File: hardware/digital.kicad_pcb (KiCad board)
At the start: 4 copper layers, 186.7 x 100 mm, 515 parts, among them J1 IPEX-1, J10 Conn_01x03_Pin, J11 Conn_01x03_Pin, J12 Conn_01x10_Pin, J14 Conn_01x03_Pin, J15 Conn_01x02_Pin, J16 Conn_01x03_Pin, J17 Micro_SD_Card_Det1, J18 Conn_01x03_Pin, J19 Micro_SD_Card_Det1, J2 IPEX-1, J20 USB_C_Receptacle_USB2.0_16P, J21 USB_C_Receptacle_USB2.0_16P, J22 USB_C_Receptacle_USB2.0_16P, J23 IPEX-1, J24 IPEX-1, J25 IPEX-1, J26 IPEX-1, J27 IPEX-1, J28 IPEX-1, J29 IPEX-1, J3 IPEX-1, J30 IPEX-1, J35 IPEX-1, J36 IPEX-1, J37 IPEX-1, J38 IPEX-1, J39 IPEX-1, J4 IPEX-1, J40 IPEX-1, J41 IPEX-1, J42 IPEX-1, J43 IPEX-1, J44 IPEX-1, J45 IPEX-1, J46 IPEX-1, J47 IPEX-1, J48 IPEX-1, J49 IPEX-1, J5 IPEX-1, J50 IPEX-1, J51 IPEX-1, J52 IPEX-1, J53 IPEX-1, J54 IPEX-1, J55 IPEX-1, J56 IPEX-1, J57 IPEX-1, J58 IPEX-1, J6 IPEX-1, J7 IPEX-1, J8 IPEX-1, J9 IPEX-1, Q1 BSC098N10NS5, Q2 BSC098N10NS5, SW1 SW_DIP_x03, SW2 SW_DIP_x03, SW3 SW_DIP_x03, SW4 SW_DIP_x03, SW5 SW_DIP_x03, SW6 SW_DIP_x03, SW7 SW_DIP_x03, U1 ICE40HX4K-TQ144, U10 LM5050-1, U11 CH224K, U12 LM5050-1, U13 CH224K, U14 TPS54302, U15 TPS7A7002DDA, U16 TPS54302, U17 TPS7A7002DDA, U18 74HC244, U19 74HC244, U2 74HC244, U20 74HC244, U21 REF5030ID, U22 MCP4728, U23 MCP4728, U24 REF5050ID, U25 MCP4728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

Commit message: route
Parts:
- removed the C62 at (66.5, 118.7)
- removed the C63 at (66.5, 122.8)
- removed the C64 at (76.0, 123.7)
- removed the C65 at (78.5, 123.2)
- removed the C66 at (43.5, 117.2)
- removed the C69 at (76.0, 139.2)
- removed the C70 at (78.5, 138.7)
- removed the C72 at (64.8, 105.8)
- removed the C73 at (59.7, 108.3)
- removed the C74 at (61.4, 108.3)
- removed the C75 at (68.3, 104.3)
- removed the C76 at (60.1, 105.2)
- removed the C77 at (60.1, 103.7)
- removed the C78 at (52.9, 99.5)
- removed the C79 at (54.6, 99.6)
- removed the C80 at (67.4, 99.5)
- removed the C81 at (64.2, 102.2)
- removed the C82 at (113.6, 212.3)
- removed the C83 at (113.6, 215.3)
- removed the C84 at (113.6, 218.4)
- removed the C85 at (64.8, 89.9)
- removed the C86 at (59.7, 92.4)
- removed the C87 at (61.4, 92.4)
- removed the C88 at (68.3, 88.4)
- removed the C89 at (60.1, 89.3)
- removed the C90 at (60.1, 87.8)
- removed the C91 at (52.8, 83.8)
- removed the C92 at (54.5, 83.8)
- removed the C93 at (67.3, 83.5)
- removed the C94 at (64.1, 86.3)
- removed the C95 at (113.6, 221.4)
- removed the C96 at (113.6, 224.4)
- removed the C97 at (113.6, 227.4)
- removed the D11 at (37.5, 118.1)
- removed the D12 at (69.5, 119.7)
- removed the D13 at (51.5, 119.2)
- removed the D14 at (48.5, 119.2)
- removed the D16 at (69.5, 134.7)
- removed the D18 at (76.5, 128.7)
- removed the J20 at (32.0, 121.2)
- removed the J23 at (100.5, 196.8)
- removed the J24 at (100.5, 206.1)
- removed the J25 at (109.9, 196.8)
- removed the J26 at (109.9, 206.1)
- removed the J27 at (119.3, 196.8)
- removed the J28 at (119.3, 206.1)
- removed the J29 at (128.7, 196.8)
- removed the J30 at (128.7, 206.1)
- removed JP3, JP4, JP5: SolderJumper_2_Open, Jumper:SolderJumper-2_P1.3mm_Open_RoundedPad1.0x1.5mm
- removed L4, L5: 10uH, Inductor_SMD:L_Changjiang_FXL0630
- removed Q1, Q2: BSC098N10NS5, Package_TO_SOT_SMD:TDSON-8-1
- removed the R52 at (50.0, 117.2)
- removed the R53 at (40.5, 117.7)
- removed the R54 at (51.5, 116.7)
- removed the R57 at (48.5, 116.7)
- removed the R58 at (53.0, 118.7)
- removed the R59 at (53.0, 121.2)
- removed the R60 at (53.0, 123.7)
- removed the R61 at (79.1, 128.7)
- removed the R69 at (67.3, 104.3)
- removed the R70 at (64.7, 99.0)
- removed the R71 at (64.7, 100.5)
- removed the R72 at (64.8, 110.8)
- removed the R73 at (66.3, 104.3)
- removed the R74 at (64.8, 104.8)
- removed the R75 at (64.7, 97.5)
- removed the R76 at (64.8, 103.8)
- removed the R77 at (67.3, 88.4)
- removed the R78 at (64.6, 82.9)
- removed the R79 at (64.6, 84.4)
- removed the R80 at (64.8, 94.9)
- removed the R81 at (66.3, 88.4)
- removed the R82 at (64.8, 88.9)
- removed the R83 at (64.6, 81.4)
- removed the R84 at (64.8, 87.9)
- removed the SW1 at (59.5, 121.2)
- removed the U10 at (73.0, 123.7)
- removed the U11 at (43.5, 121.2)
- removed the U12 at (73.0, 139.2)
- removed the U14 at (64.8, 108.3)
- removed the U15 at (59.2, 99.5)
- removed the U16 at (64.8, 92.4)
- removed the U17 at (59.1, 83.5)
- moved R24 54.4 mm to (91.5, 104.1), turned to -90 degrees
- moved C29 52.3 mm to (91.5, 92.0), turned to 0 degrees
- moved JP1 52.0 mm to (89.7, 104.2), turned to 90 degrees
- moved C28 51.9 mm to (91.5, 95.8), turned to 0 degrees
- moved C34 49.5 mm to (89.0, 88.5), turned to 90 degrees
- moved R28 48.9 mm to (88.8, 101.0), turned to 90 degrees
- moved C33 48.1 mm to (88.0, 88.5), turned to 90 degrees
- moved C40 47.8 mm to (87.4, 104.1), turned to 90 degrees
- moved C32 47.3 mm to (84.2, 79.6), turned to 90 degrees
- moved R26 46.7 mm to (87.0, 88.5), turned to -90 degrees
- moved C24 46.2 mm to (86.9, 101.0), turned to -90 degrees
- moved R25 45.3 mm to (86.0, 88.5), turned to -90 degrees
- moved C31 44.8 mm to (85.9, 101.0), turned to -90 degrees
- moved JP2 44.7 mm to (81.8, 79.3), turned to 180 degrees
- moved Y1 44.3 mm to (84.8, 104.1), turned to 0 degrees
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- renumbered C6 to C10, C130 to C100, C131 to C101, C132 to C102, C133 to C103, C134 to C104, C135 to C105, C136 to C106, C137 to C107, C138 to C108, C139 to C109, C7 to C11, C140 to C110, C141 to C111, C142 to C112, C143 to C113, C144 to C114, C145 to C115, C146 to C116, C149 to C12, C8 to C13, C10 to C14, C11 to C15, C13 to C16, C14 to C17, C15 to C18, C16 to C19, C17 to C20, C18 to C21, C19 to C22, C20 to C23, C21 to C24, C22 to C25, C23 to C26, C24 to C27, C25 to C28, C26 to C29, C148 to C3, C27 to C30, C28 to C31, C29 to C32, C30 to C33, C31 to C34, C32 to C35, C33 to C36, C34 to C37, C35 to C38, C36 to C39, C3 to C4, C37 to C40, C38 to C41, C39 to C42, C40 to C43, C41 to C44, C42 to C45, C43 to C46, C44 to C47, C45 to C48, C46 to C49, C147 to C5, C47 to C50, C48 to C51, C49 to C52, C50 to C53, C51 to C54, C52 to C55, C53 to C56, C54 to C57, C55 to C58, C56 to C59, C4 to C6, C57 to C60, C58 to C61, C59 to C62, C60 to C63, C61 to C64, C67 to C65, C68 to C66, C71 to C67, C98 to C68, C99 to C69, C12 to C7, C100 to C70, C101 to C71, C102 to C72, C103 to C73, C104 to C74, C105 to C75, C106 to C76, C107 to C77, C108 to C78, C109 to C79, C5 to C8, C110 to C80, C111 to C81, C112 to C82, C113 to C83, C114 to C84, C115 to C85, C116 to C86, C117 to C87, C118 to C88, C119 to C89, C120 to C90, C121 to C91, C122 to C92, C123 to C93, C124 to C94, C125 to C95, C126 to C96, C127 to C97, C128 to C98, C129 to C99, D15 to D10, D17 to D11, D19 to D12, D10 to D13, D20 to D14, D21 to D15, D22 to D16, D23 to D17, D24 to D18, D25 to D19, D26 to D20, D27 to D21, D28 to D22, D29 to D23, D30 to D24, D31 to D25, D32 to D26, D33 to D27, D34 to D28, D35 to D29, D36 to D30, D37 to D31, D38 to D32, D39 to D33, D40 to D34, D41 to D35, D42 to D36, D43 to D37, J14 to J13, J15 to J14, J16 to J15, J17 to J16, J18 to J17, J19 to J18, J22 to J19, J21 to J20, J35 to J21, J36 to J22, J37 to J23, J38 to J24, J39 to J25, J40 to J26, J41 to J27, J42 to J28, J43 to J29, J44 to J30, J45 to J31, J46 to J32, J47 to J33, J48 to J34, J49 to J35, J50 to J36, J51 to J37, J52 to J38, J53 to J39, J54 to J40, J55 to J41, J56 to J42, J57 to J43, J58 to J44, R124 to R100, R125 to R101, R126 to R102, R127 to R103, R128 to R104, R129 to R105, R130 to R106, R131 to R107, R132 to R108, R133 to R109, R134 to R110, R135 to R111, R136 to R112, R137 to R113, R138 to R114, R139 to R115, R140 to R116, R141 to R117, R142 to R118, R143 to R119, R144 to R120, R145 to R121, R146 to R122, R147 to R123, R148 to R124, R149 to R125, R150 to R126, R151 to R127, R152 to R128, R153 to R129, R154 to R130, R155 to R131, R156 to R132, R157 to R133, R158 to R134, R159 to R135, R160 to R136, R62 to R51, R63 to R52, R64 to R53, R65 to R54, R66 to R55, R67 to R56, R68 to R57, R51 to R58, R55 to R59, R56 to R60, R85 to R61, R86 to R62, R87 to R63, R88 to R64, R89 to R65, R90 to R66, R91 to R67, R92 to R68, R93 to R69, R94 to R70, R95 to R71, R96 to R72, R97 to R73, R98 to R74, R99 to R75, R100 to R76, R101 to R77, R102 to R78, R103 to R79, R104 to R80, R105 to R81, R106 to R82, R107 to R83, R108 to R84, R109 to R85, R110 to R86, R111 to R87, R112 to R88, R113 to R89, R114 to R90, R115 to R91, R116 to R92, R117 to R93, R118 to R94, R119 to R95, R120 to R96, R121 to R97, R122 to R98, R123 to R99, SW2 to SW1, SW3 to SW2, SW4 to SW3, SW5 to SW4, SW6 to SW5, SW7 to SW6, TP43 to TP1, TP22 to TP10, TP4 to TP11, TP23 to TP12, TP24 to TP13, TP5 to TP14, TP25 to TP15, TP6 to TP16, TP26 to TP17, TP7 to TP18, TP27 to TP19, TP44 to TP2, TP28 to TP20, TP29 to TP21, TP30 to TP22, TP8 to TP23, TP16 to TP24, TP9 to TP25, TP31 to TP26, TP10 to TP27, TP32 to TP28, TP33 to TP29, TP1 to TP3, TP34 to TP30, TP11 to TP31, TP35 to TP32, TP36 to TP33, TP12 to TP34, TP37 to TP35, TP13 to TP36, TP38 to TP37, TP14 to TP38, TP18 to TP4, TP15 to TP43, TP17 to TP44, TP2 to TP5, TP3 to TP6, TP19 to TP7, TP20 to TP8, TP21 to TP9, U13 to U10, U18 to U11, U19 to U12, U20 to U13, U21 to U14, U22 to U15, U23 to U16, U24 to U17, U25 to U18, U26 to U19, U27 to U20, U28 to U21, U29 to U22, U30 to U23, U31 to U24, U32 to U25, U33 to U26, U34 to U27, U35 to U28, U36 to U29, U37 to U30, U38 to U31, U39 to U32, U40 to U33, U41 to U34, U42 to U35, U43 to U36, U44 to U37, U45 to U38
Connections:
- C65 pad 1: Net-(D15-K) -> +20V
- C66 pad 1: Net-(D15-K) -> +20V
- D10 pad 1: Net-(D15-K) -> +20V
- J19 pad A4: Net-(D15-K) -> +20V
- J19 pad A9: Net-(D15-K) -> +20V
- J19 pad B4: Net-(D15-K) -> +20V
- J19 pad B9: Net-(D15-K) -> +20V
- R51 pad 1: Net-(D15-K) -> +20V
- R52 pad 1: Net-(D15-K) -> +20V
- R53 pad 1: Net-(D15-K) -> +20V
- U4 pad 4: /MCU/~{LDAC}0 -> /MCU/~{LDAC}5
- U4 pad 5: /MCU/~{LDAC}1 -> /MCU/~{LDAC}4
- U4 pad 6: /MCU/~{LDAC}2 -> /MCU/~{LDAC}3
- U4 pad 7: /MCU/~{LDAC}3 -> /MCU/~{LDAC}2
- U4 pad 8: /MCU/~{LDAC}4 -> /MCU/~{LDAC}1
- U4 pad 9: /MCU/~{LDAC}5 -> /MCU/~{LDAC}0
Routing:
- net /MCU/~{LDAC}2: track 0.00 -> 118.8 mm, vias 0 -> 2
- net /MCU/~{LDAC}3: track 0.00 -> 111.4 mm, vias 0 -> 2
- net /MCU/~{LDAC}1: track 0.00 -> 108.2 mm, vias 0 -> 2
- net /MCU/~{LDAC}4: track 0.00 -> 106.4 mm, vias 0 -> 2
- net +5V5_A: track 0.00 -> 98.8 mm
- net /MCU/~{LDAC}0: track 0.00 -> 85.9 mm, vias 0 -> 2
- net /MCU/~{LDAC}5: track 0.00 -> 80.4 mm, vias 0 -> 2
- net /MCU/SD_SO: track 0.00 -> 50.9 mm, vias 0 -> 3
- net /FPGA/GBIN2: track 0.00 -> 49.0 mm, vias 0 -> 2
- net /FPGA/D3: track 0.00 -> 39.2 mm, vias 0 -> 2
- net /FPGA/CDONE: track 0.00 -> 37.5 mm, vias 0 -> 2
- net /FPGA/D1: track 0.00 -> 37.4 mm, vias 0 -> 2
- net /MCU/SD_SI: track 0.00 -> 36.6 mm, vias 0 -> 2
- net /FPGA/~{RESET}: track 0.00 -> 36.4 mm, vias 0 -> 2
- net /FPGA/D2: track 0.00 -> 36.0 mm, vias 0 -> 2
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
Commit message: route all signal
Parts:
- removed A1: RaspberryPi_Pico, Module:RaspberryPi_Pico_SMD_HandSolder
- removed R79: 0R, Resistor_SMD:R_0402_1005Metric
- added J45: Conn_01x24_Pin, Connector_PinHeader_2.54mm:PinHeader_1x24_P2.54mm_Vertical, F.Cu at (137.2, 56.0)
- added TP45: TestPoint, TestPoint:TestPoint_Pad_D1.0mm, B.Cu at (117.0, 87.0)
- added TP46: TestPoint, TestPoint:TestPoint_Pad_D1.0mm, B.Cu at (115.0, 87.0)
- moved TP4 42.5 mm to (181.0, 115.0)
- moved TP24 42.4 mm to (181.0, 85.0), turned to -90 degrees
- moved R17 25.4 mm to (108.2, 97.5), turned to 180 degrees
- moved C97 6.52 mm to (151.0, 74.8), turned to 90 degrees
- moved TP44 6.21 mm to (98.4, 109.7)
- moved C80 5.48 mm to (179.0, 125.2), turned to -90 degrees
- moved C79 5.10 mm to (176.0, 123.0), turned to 180 degrees
- moved C89 4.49 mm to (190.2, 86.0), turned to 0 degrees
- moved TP7 2.94 mm to (139.5, 128.9), turned to 146.25 degrees
- moved TP19 2.76 mm to (193.8, 125.2), turned to -123.75 degrees
- moved TP8 2.69 mm to (148.0, 134.5), turned to 146.25 degrees
- moved C77 2.14 mm to (155.0, 125.2), turned to -90 degrees
- moved TP13 2.02 mm to (177.0, 136.2), turned to -168.75 degrees
- moved TP20 2.02 mm to (199.2, 117.0), turned to -123.75 degrees
- moved J1 1.97 mm to (116.5, 117.5)
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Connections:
- net /debug/CH_0 renamed Net-(U11-1Y0)
- net /debug/CH_1 renamed Net-(U11-1Y1)
- net /debug/CH_10 renamed Net-(U12-1Y2)
- net /debug/CH_11 renamed Net-(U12-1Y3)
- net /debug/CH_12 renamed Net-(U12-2Y0)
- net /debug/CH_13 renamed Net-(U12-2Y1)
- net /debug/CH_14 renamed Net-(U12-2Y2)
- net /debug/CH_15 renamed Net-(U12-2Y3)
- net /debug/CH_16 renamed Net-(U13-1Y0)
- net /debug/CH_17 renamed Net-(U13-1Y1)
- net /debug/CH_18 renamed Net-(U13-1Y2)
- net /debug/CH_19 renamed Net-(U13-1Y3)
- net /debug/CH_2 renamed Net-(U11-1Y2)
- net /debug/CH_20 renamed Net-(U13-2Y0)
- net /debug/CH_21 renamed Net-(U13-2Y1)
- net /debug/CH_22 renamed Net-(U13-2Y2)
- net /debug/CH_23 renamed Net-(U13-2Y3)
- net /debug/CH_3 renamed Net-(U11-1Y3)
- net /debug/CH_4 renamed Net-(U11-2Y0)
- net /debug/CH_5 renamed Net-(U11-2Y1)
- net /debug/CH_6 renamed Net-(U11-2Y2)
- net /debug/CH_7 renamed Net-(U11-2Y3)
- net /debug/CH_8 renamed Net-(U12-1Y0)
- net /debug/CH_9 renamed Net-(U12-1Y1)
- C68 pad 2: +3V3_DEBUG -> +3V3
- C69 pad 2: +3V3_DEBUG -> +3V3
- C70 pad 2: +3V3_DEBUG -> +3V3
- C71 pad 2: +3V3_DEBUG -> +3V3
- C72 pad 2: +3V3_DEBUG -> +3V3
- C73 pad 2: +3V3_DEBUG -> +3V3
- U1 pad 33: /FPGA/DEBUG_TRIG_0 -> Net-(U1D-IOL_25A)
- U1 pad 34: /FPGA/DEBUG_TRIG_1 -> Net-(U1D-IOL_25B)
- U11 pad 20: +3V3_DEBUG -> +3V3
- U12 pad 20: +3V3_DEBUG -> +3V3
- U13 pad 20: +3V3_DEBUG -> +3V3
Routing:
- net /MCU/VREF_SDA: track 2.60 -> 213.6 mm, vias 0 -> 7
- net /MCU/VREF_SCL: track 2.35 -> 209.4 mm, vias 0 -> 7
- net /FPGA/DEBUG_0: track 0.00 -> 60.3 mm, vias 0 -> 2
- net /FPGA/DEBUG_1: track 0.00 -> 58.8 mm, vias 0 -> 2
- net /FPGA/DEBUG_2: track 0.00 -> 57.7 mm, vias 0 -> 2
- net /FPGA/DEBUG_23: track 0.00 -> 57.6 mm, vias 0 -> 2
- net /FPGA/DEBUG_3: track 0.00 -> 56.7 mm, vias 0 -> 2
- net /FPGA/DEBUG_22: track 0.00 -> 55.9 mm, vias 0 -> 2
- net /FPGA/DEBUG_21: track 0.00 -> 54.3 mm, vias 0 -> 2
- net /FPGA/DEBUG_20: track 0.00 -> 53.8 mm, vias 0 -> 2
- net /FPGA/DEBUG_19: track 0.00 -> 53.7 mm, vias 0 -> 2
- net /FPGA/DEBUG_18: track 0.00 -> 53.2 mm, vias 0 -> 2
- net /FPGA/DEBUG_4: track 0.00 -> 52.6 mm, vias 0 -> 2
- net /FPGA/DEBUG_17: track 0.00 -> 52.3 mm, vias 0 -> 2
- net /FPGA/DEBUG_16: track 0.00 -> 51.6 mm, vias 0 -> 2
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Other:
- board size 186.7 x 100 mm -> 162.2 x 100 mm

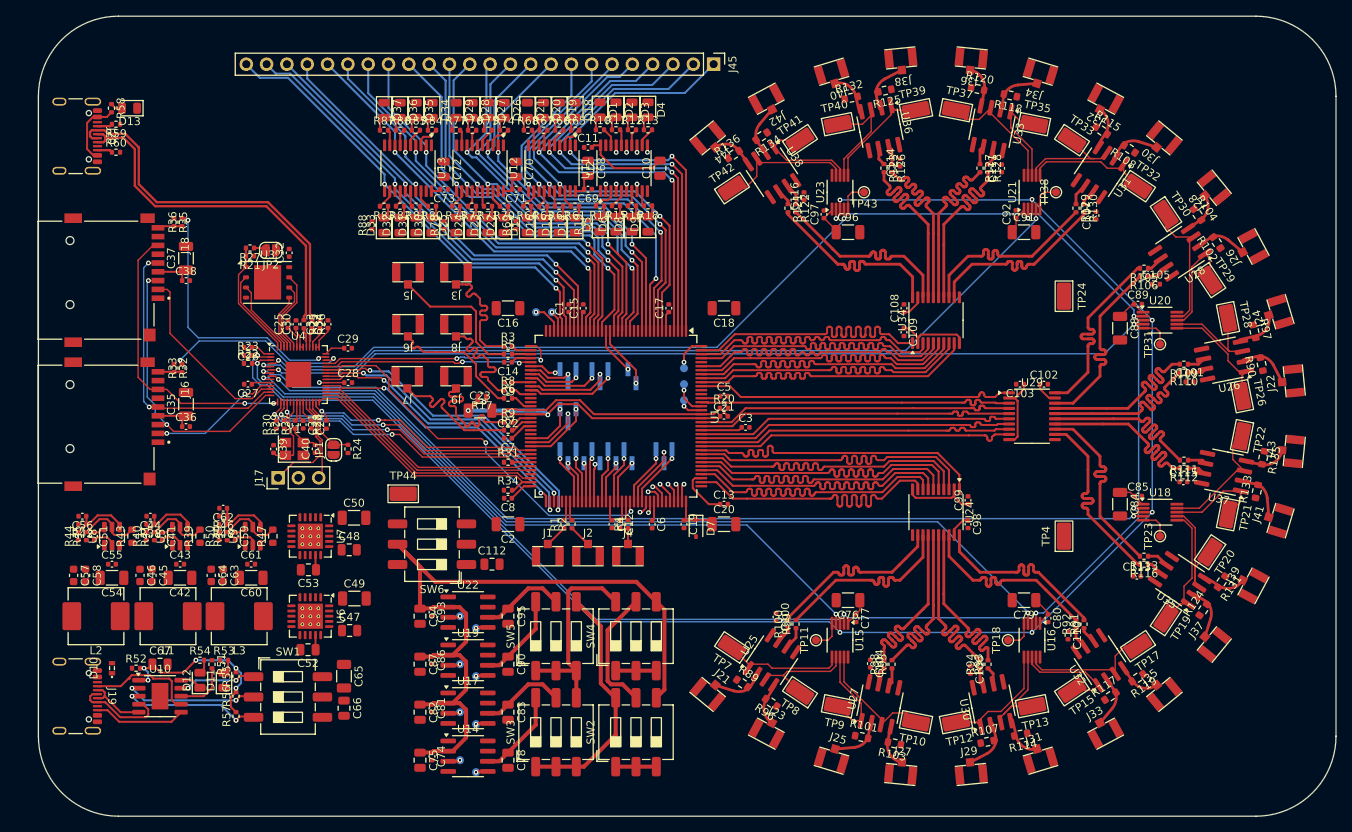
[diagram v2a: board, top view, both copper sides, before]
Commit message: add board edge
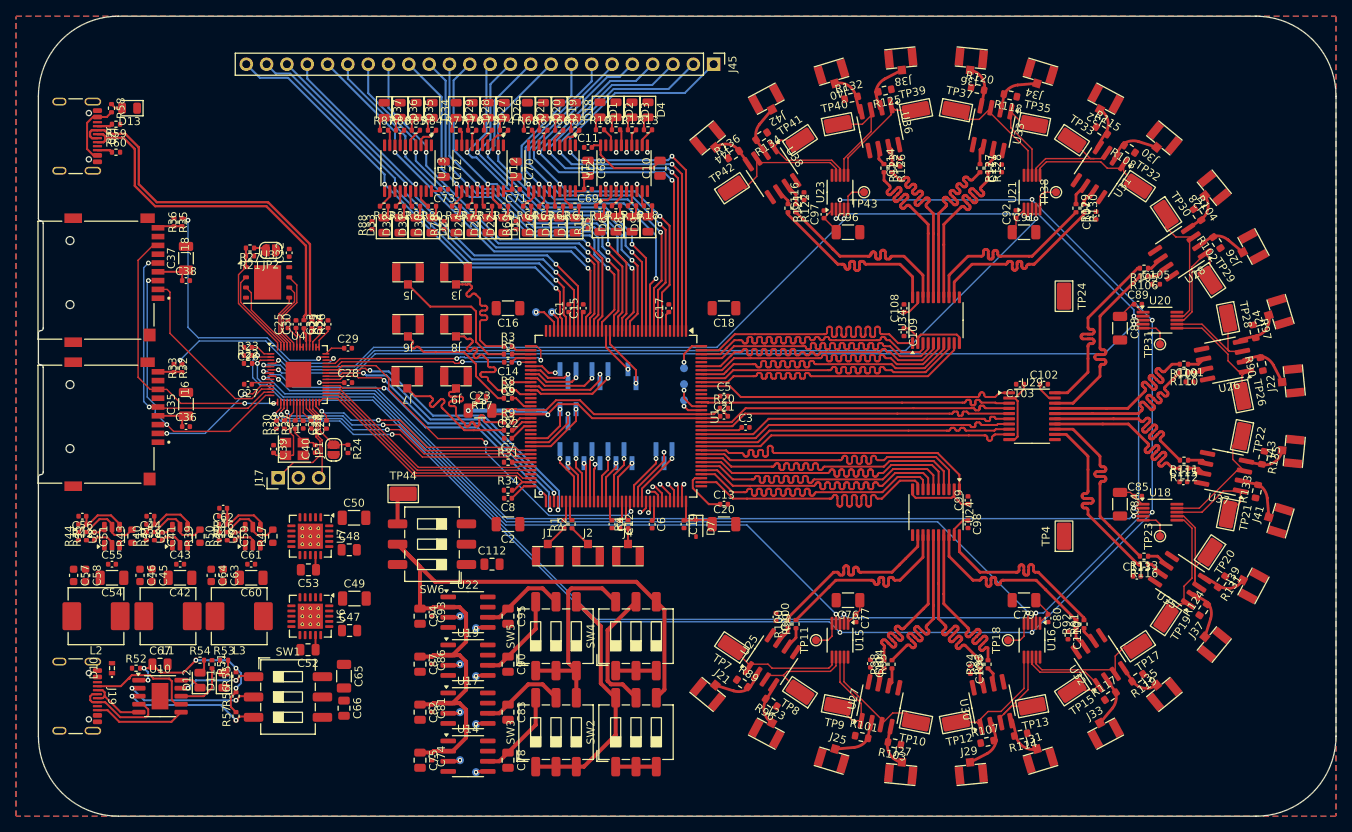
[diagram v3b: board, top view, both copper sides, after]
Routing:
- net Net-(SW6-Pad4): track 0.00 -> 4.05 mm
- added copper zone on B.Cu, net GND
- added copper zone on F.Cu, net GND
- added copper zone on In1.Cu, net GND
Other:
- outline, holes or cut-outs redrawn
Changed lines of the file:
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@@
 	)
 	(gr_arc
+		(start 53.4 107)
+		(mid 53.312132 107.212132)
+		(end 53.1 107.3)
+		(stroke
+			(width 0.05)
+			(type default)
+		)
+		(layer "Edge.Cuts")
+	)
+	(gr_arc
 		(start 52.8 60)
 		(mid 55.728932 52.928932)
@@
 	(gr_line
 		(start 52.8 60)
-		(end 52.8 140)
+		(end 52.8 75.3)
+		(stroke
+			(width 0.05)
+			(type default)
+		)
+		(layer "Edge.Cuts")
+	)
+	(gr_arc
+		(start 52.8 107.6)
+		(mid 52.887868 107.387868)
+		(end 53.1 107.3)
+		(stroke
+			(width 0.05)
+			(type default)
+		)
+		(layer "Edge.Cuts")
+	)
+	(gr_arc
+		(start 53.1 75.6)
+		(mid 52.887868 75.512132)
+		(end 52.8 75.3)
+		(stroke
+			(width 0.05)
+			(type default)
+		)
+		(layer "Edge.Cuts")
+	)
+	(gr_arc
+		(start 53.4 89)
+		(mid 53.312132 89.212132)
+		(end 53.1 89.3)
+		(stroke
+			(width 0.05)
+			(type default)
+		)
+		(layer "Edge.Cuts")
+	)
+	(gr_line
+		(start 53.4 75.9)
+		(end 53.4 89)
 		(stroke
 			(width 0.05)
 			(type default)
 		)
-		(locked yes)
 		(layer "Edge.Cuts")
 	)
@@
 		(layer "Edge.Cuts")
 	)
+	(gr_line
+		(start 52.8 107.6)
+		(end 52.8 140)
+		(stroke
+			(width 0.05)
+			(type default)
+		)
+		(layer "Edge.Cuts")
+	)
 	(gr_arc
 		(start 205 50)
@@
 		(layer "Edge.Cuts")
 	)
+	(gr_arc
+		(start 52.8 89.6)
+		(mid 52.887868 89.387868)
+		(end 53.1 89.3)
+		(stroke
+			(width 0.05)
+			(type default)
+		)
+		(layer "Edge.Cuts")
+	)
+	(gr_arc
+		(start 53.1 93.6)
+		(mid 53.312132 93.687868)
+		(end 53.4 93.9)
+		(stroke
+			(width 0.05)
+			(type default)
+		)
+		(layer "Edge.Cuts")
+	)
+	(gr_line
+		(start 52.8 89.6)
+		(end 52.8 93.3)
+		(stroke
+			(width 0.05)
+			(type default)
+		)
+		(layer "Edge.Cuts")
+	)
 	(gr_line
 		(start 215 140)
@@
 		(layer "Edge.Cuts")
 	)
+	(gr_line
+		(start 53.4 93.9)
+		(end 53.4 107)
+		(stroke
+			(width 0.05)
+			(type default)
+		)
+		(layer "Edge.Cuts")
+	)
 	(gr_arc
 		(start 215 140)
@@
 		(layer "Edge.Cuts")
 	)
+	(gr_arc
+		(start 53.1 75.6)
+		(mid 53.312132 75.687868)
+		(end 53.4 75.9)
+		(stroke
+			(width 0.05)
+			(type default)
+		)
+		(layer "Edge.Cuts")
+	)
+	(gr_arc
+		(start 53.1 93.6)
+		(mid 52.887868 93.512132)
+		(end 52.8 93.3)
+		(stroke
+			(width 0.05)
+			(type default)
+		)
+		(layer "Edge.Cuts")
+	)
 	(segment
 		(start 117.75 89.3375)
@@
 	)
 	(segment
+		(start 97.695 110.405)
+		(end 97.695 113.46)
+		(width 0.508)
+		(layer "F.Cu")
+		(net 392)
+	)
+	(segment
+		(start 98.4 109.7)
+		(end 97.695 110.405)
+		(width 0.508)
+		(layer "F.Cu")
+		(net 392)
+	)
+	(segment
 		(start 105.365 143.135)
 		(end 105.5 143)
@@
 		(net 405)
 	)
+	(zone
+		(net 1)
+		(net_name "GND")
+		(layers "F.Cu" "B.Cu" "In1.Cu")
+		(hatch edge 0.5)
+		(connect_pads yes
+			(clearance 0.2)
+		)
+		(min_thickness 0.2)
+		(filled_areas_thickness no)
+		(fill
+			(thermal_gap 0.5)
+			(thermal_bridge_width 0.5)
+		)
+		(polygon
+			(pts
+				(xy 50 50) (xy 215 50) (xy 215 150) (xy 50 150)
+			)
+		)
+	)
 	(generated
